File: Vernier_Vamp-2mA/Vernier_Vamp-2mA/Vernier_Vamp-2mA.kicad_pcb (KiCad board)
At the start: 4 copper layers, 143 x 99.5 mm, 185 parts, among them J1 Conn_01x02, J2 RJ45, J3 Screw_Terminal_01x04, J4 Conn_02x07_Odd_Even, J5 Conn_Coaxial, J6 Conn_Coaxial, J7 Conn_Coaxial, Q1 Si4447ADY, Q2 IRF8707PbF, SW1 DPDT_Hirose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

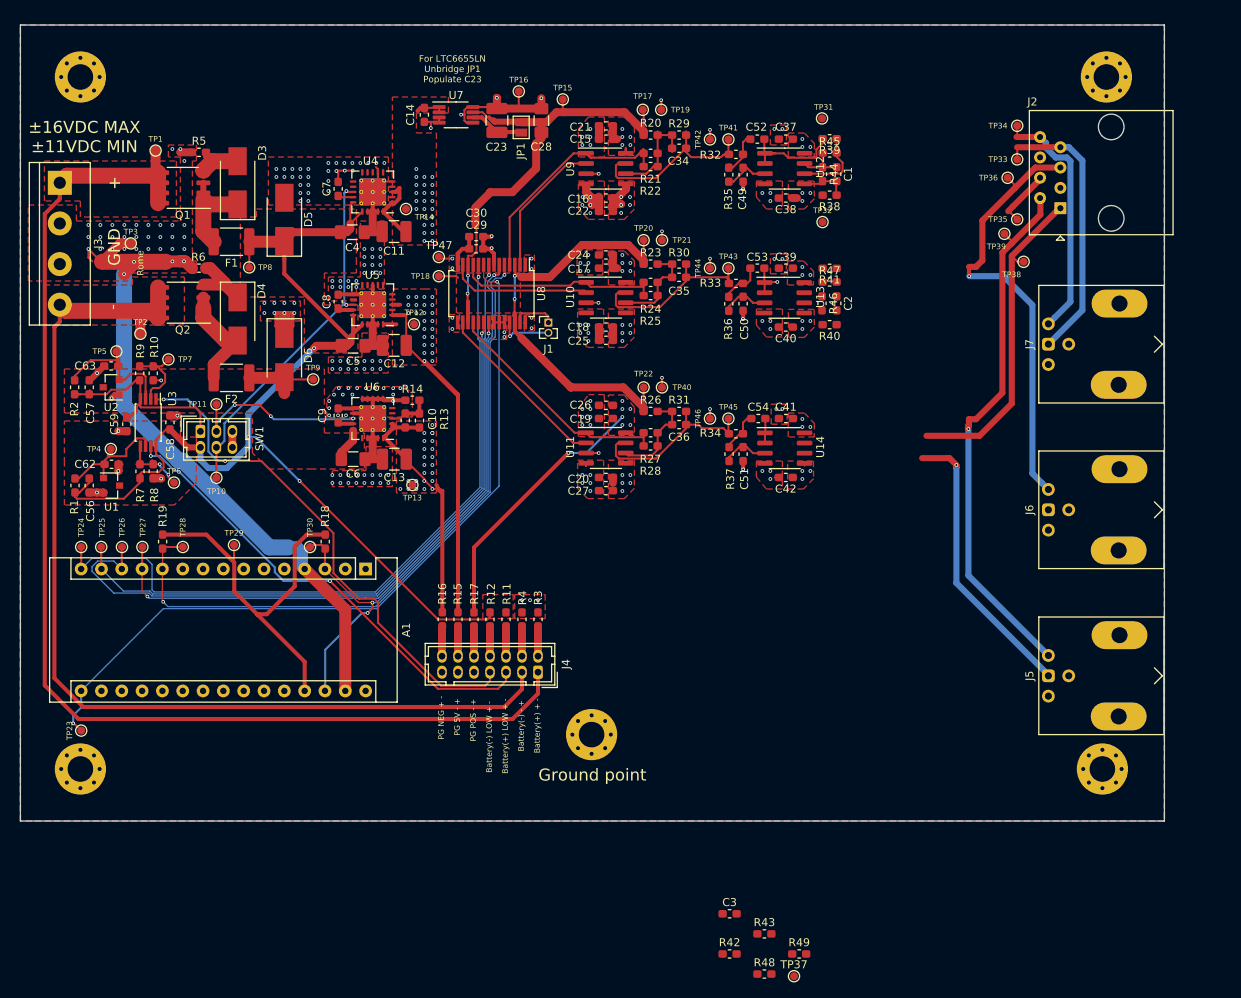
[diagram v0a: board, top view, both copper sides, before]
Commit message: 2 mA version changes
2 mA version layout had been finalised
-Board had been shortened to improve signal integrity
-Power routing optimised
-Minor fixes
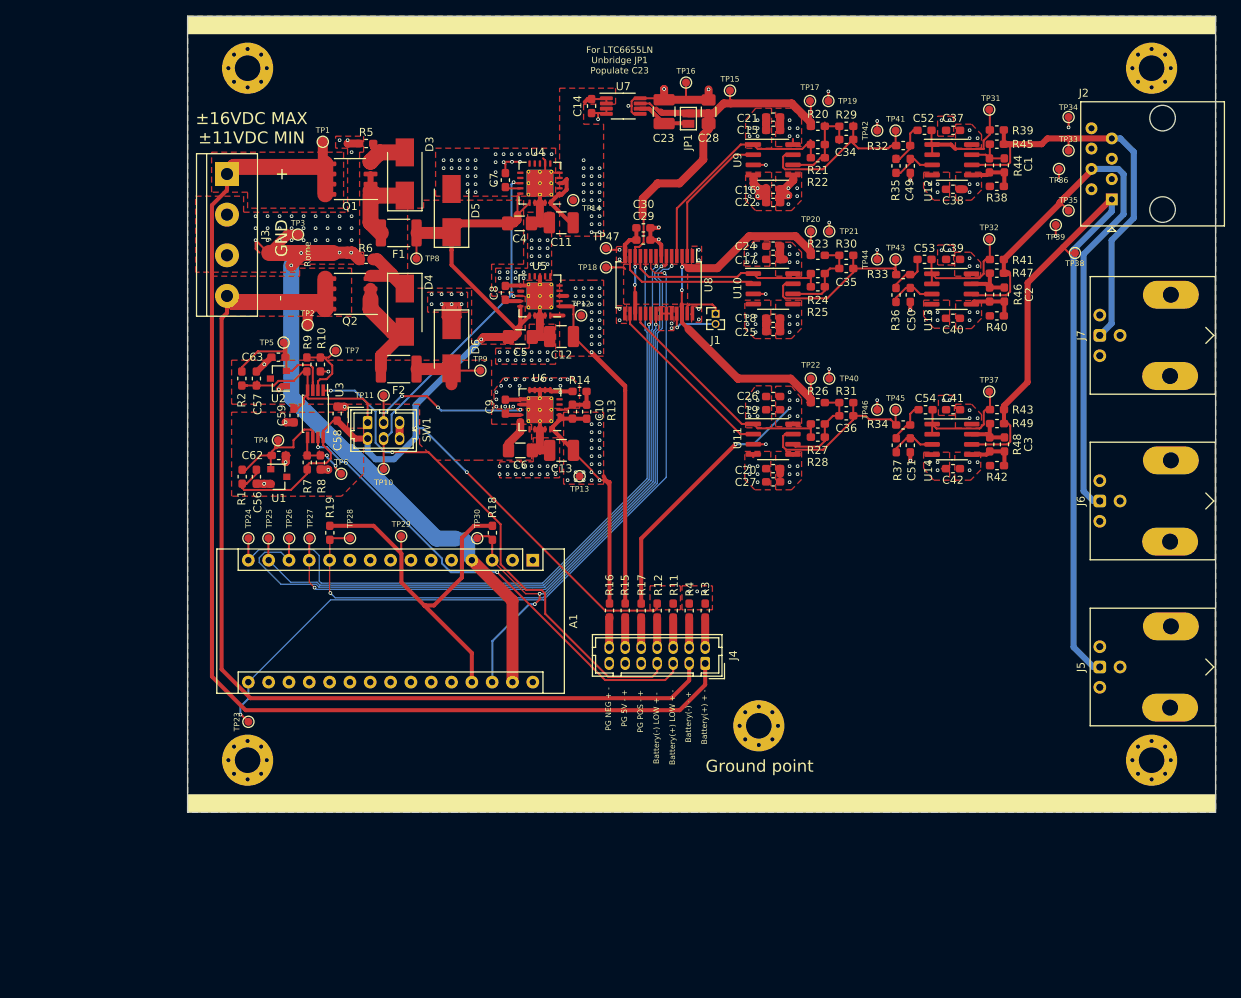
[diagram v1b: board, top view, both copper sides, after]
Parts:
- moved TP37 77.0 mm to (164.6, 93.6)
- moved R48 71.9 mm to (164.7, 100.2), turned to 270 degrees
- moved R43 71.7 mm to (165.6, 95.8), turned to 180 degrees
- moved R49 70.8 mm to (165.6, 97.6)
- moved R42 69.6 mm to (165.6, 102.8), turned to 180 degrees
- moved C3 68.0 mm to (166.5, 100.2), turned to 270 degrees
- moved R46 21.0 mm to (164.7, 81.4)
- moved C2 21.0 mm to (166.5, 81.4)
- moved C1 21.0 mm to (166.5, 65.3)
- moved TP32 20.9 mm to (164.6, 74.5)
- moved C15 20.9 mm to (137.6, 60.9)
- moved C16 20.9 mm to (137.6, 68.3)
- moved C17 20.9 mm to (137.6, 77.0)
- moved C18 20.9 mm to (137.6, 84.4)
- moved C19 20.9 mm to (137.6, 95.8)
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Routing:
- net GND: track 307.2 -> 156.2 mm, vias 224 -> 225
- net /Channel_Outputs/Coil_Iout_2: track 7.69 -> 76.0 mm
- net /Channel_Outputs/Coil_Iout_3: track 76.9 -> 105.6 mm, vias 1 -> 0
- net Net-(C54-Pad1): track 3.09 -> 14.8 mm
- net Net-(C53-Pad1): track 4.69 -> 15.1 mm, vias 1 -> 0
- net /Channel_Outputs/Coil_Iout_1: track 44.3 -> 54.1 mm
- net Net-(C2-Pad1): track 0.00 -> 6.10 mm
- net Net-(C2-Pad2): track 0.00 -> 6.07 mm
- net Net-(C3-Pad1): track 0.00 -> 5.99 mm
- net Net-(C3-Pad2): track 0.29 -> 6.05 mm
- net Net-(C52-Pad1): track 13.7 -> 16.3 mm
- net +8V: track 53.7 -> 52.6 mm
- net Net-(C1-Pad2): track 5.92 -> 6.51 mm
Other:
- board size 143 x 99.5 mm -> 128.5 x 99.5 mm
